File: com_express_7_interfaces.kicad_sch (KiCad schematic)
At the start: 8 parts, among them J11 Plug_Bus_CE7_EPT_401-51501-51

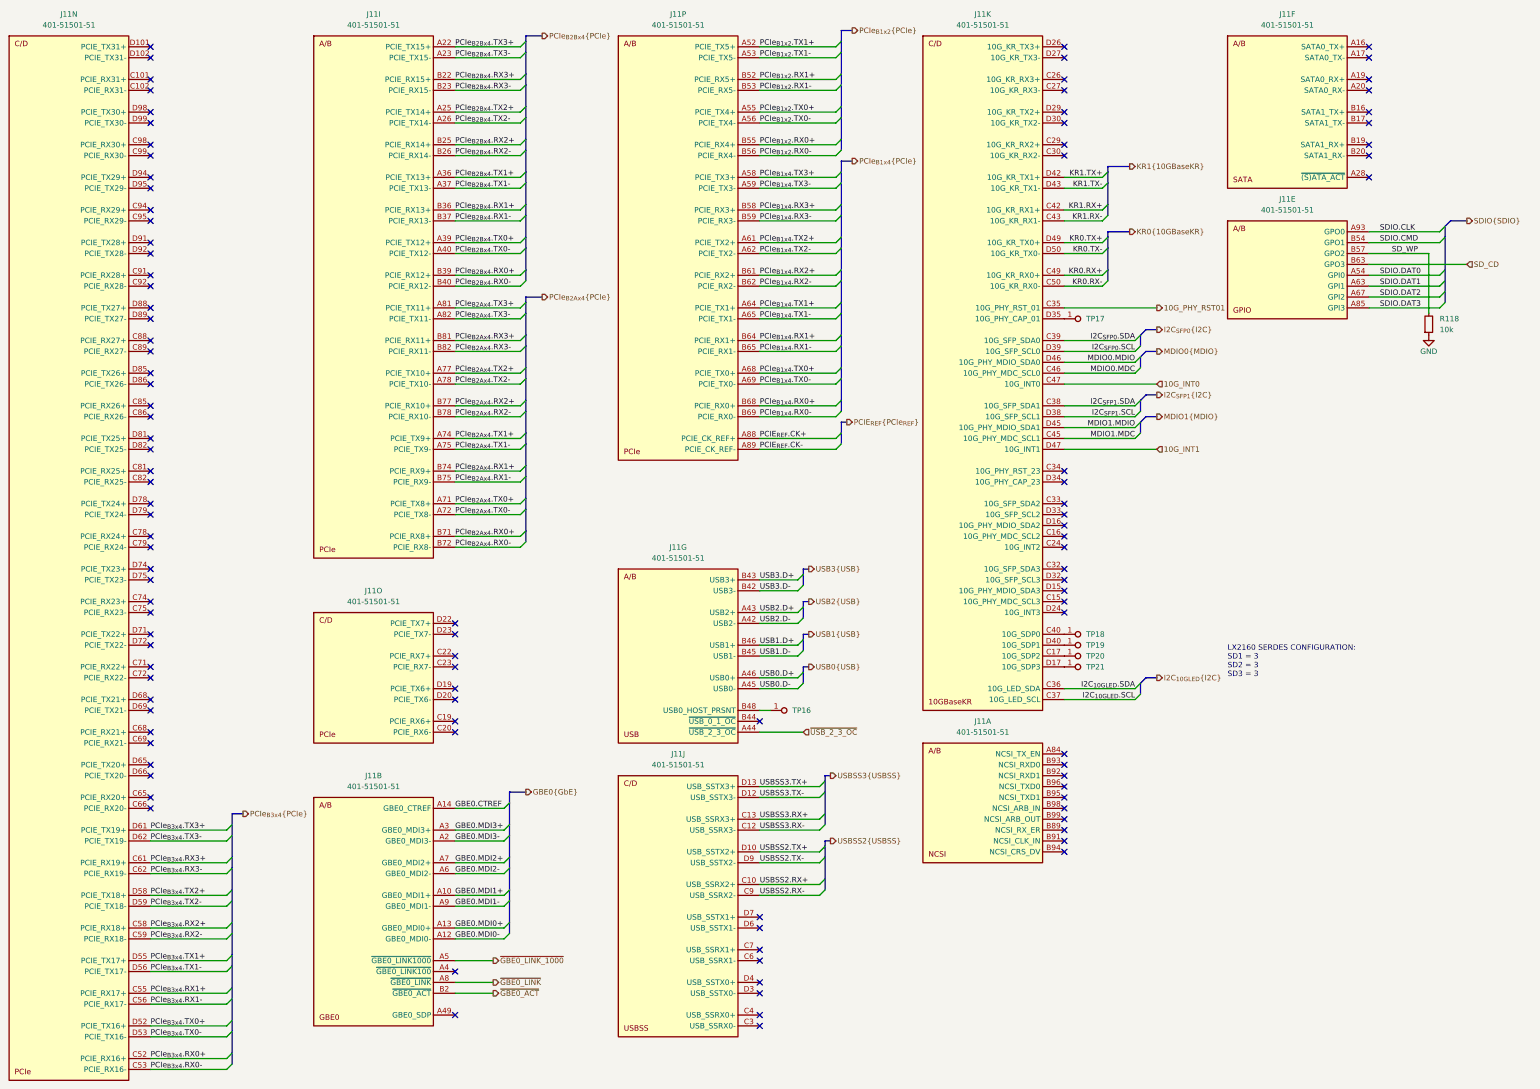
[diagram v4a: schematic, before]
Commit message: Reannotate schematic
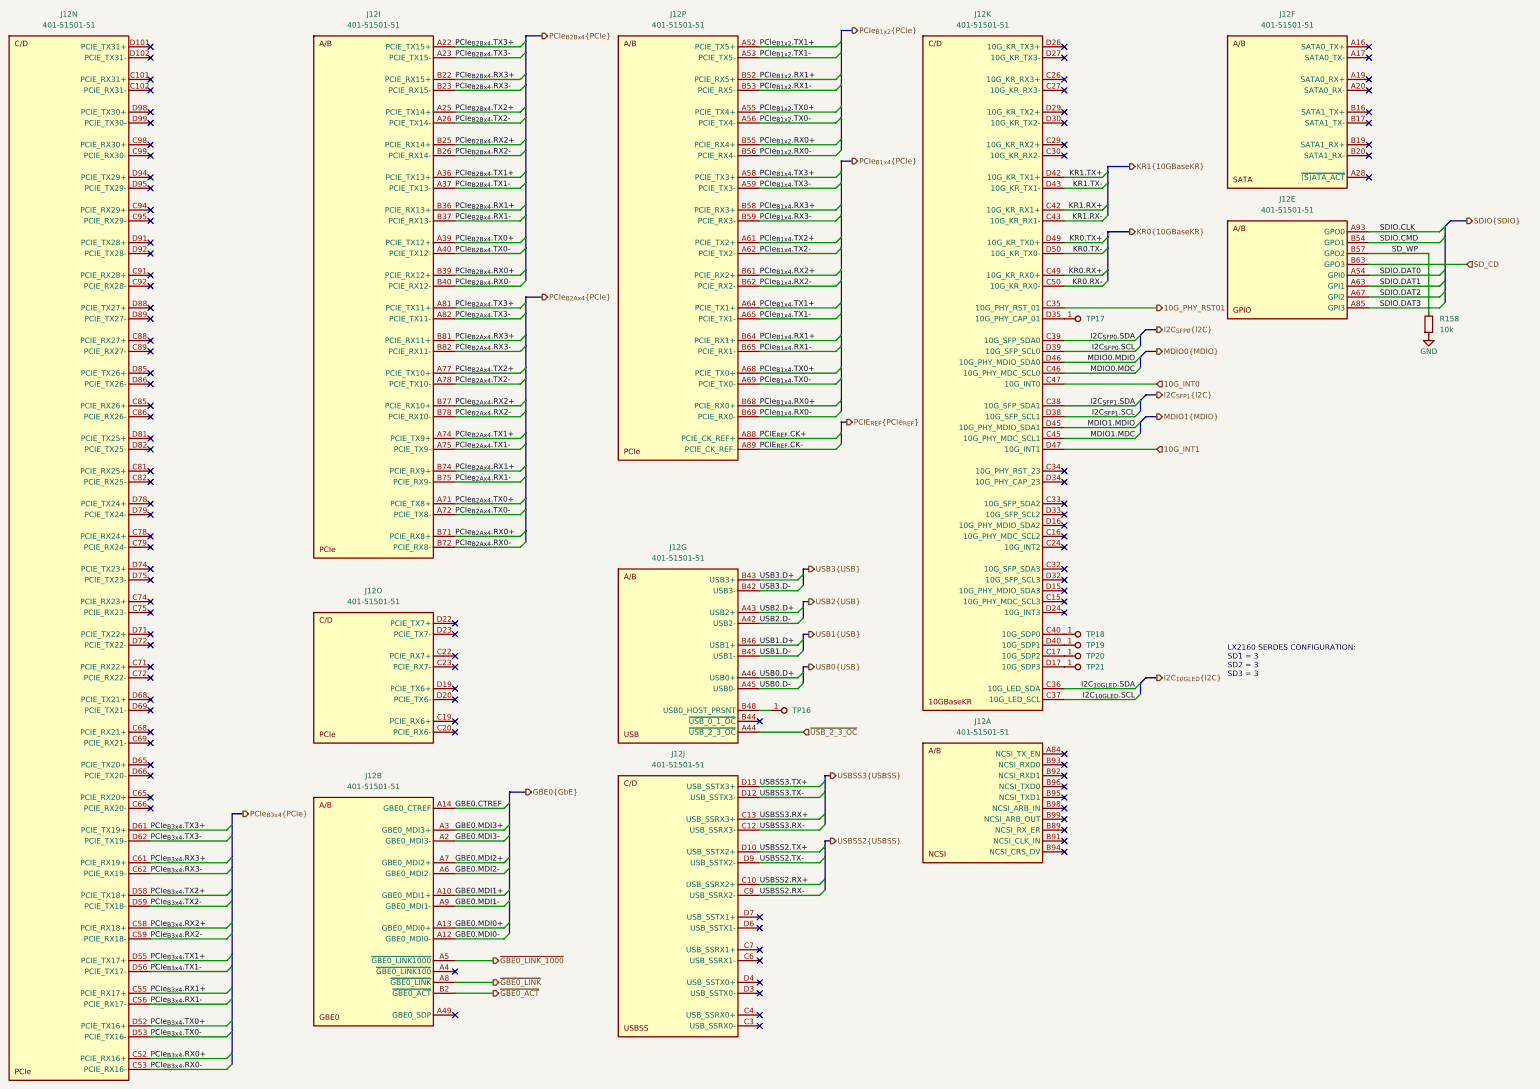
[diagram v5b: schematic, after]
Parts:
- renumbered J11 to J12, R118 to R158
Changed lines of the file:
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@@
   (symbol (lib_id "antmicroB2BConnectors:Plug_Bus_CE7_EPT_401-51501-51") (at 281.94 198.12 0) (unit 1)
     (in_bom yes) (on_board yes) (dnp no) (fields_autoplaced)
-    (property "Reference" "J11" (at 262.89 190.5 0)
+    (property "Reference" "J12" (at 262.89 190.5 0)
       (effects (font (size 1.27 1.27) (thickness 0.15)))
     )
@@
       (project "com-express-7-baseboard"
         (path "/1b8c34da-dad5-4b0b-8c4b-45db766c4dfa/d0206463-9f0a-4ce9-a6c7-202004597ed5"
-          (reference "J11") (unit 1)
+          (reference "J12") (unit 1)
         )
       )
@@
   (symbol (lib_id "antmicroB2BConnectors:Plug_Bus_CE7_EPT_401-51501-51") (at 281.94 33.02 0) (unit 11)
     (in_bom yes) (on_board yes) (dnp no) (fields_autoplaced)
-    (property "Reference" "J11" (at 262.89 25.4 0)
+    (property "Reference" "J12" (at 262.89 25.4 0)
       (effects (font (size 1.27 1.27) (thickness 0.15)))
     )
@@
       (project "com-express-7-baseboard"
         (path "/1b8c34da-dad5-4b0b-8c4b-45db766c4dfa/d0206463-9f0a-4ce9-a6c7-202004597ed5"
-          (reference "J11") (unit 11)
+          (reference "J12") (unit 11)
         )
       )
@@
   (symbol (lib_id "antmicroB2BConnectors:Plug_Bus_CE7_EPT_401-51501-51") (at 139.7 210.82 0) (unit 2)
     (in_bom yes) (on_board yes) (dnp no) (fields_autoplaced)
-    (property "Reference" "J11" (at 120.65 203.2 0)
+    (property "Reference" "J12" (at 120.65 203.2 0)
       (effects (font (size 1.27 1.27) (thickness 0.15)))
     )
@@
       (project "com-express-7-baseboard"
         (path "/1b8c34da-dad5-4b0b-8c4b-45db766c4dfa/d0206463-9f0a-4ce9-a6c7-202004597ed5"
-          (reference "J11") (unit 2)
+          (reference "J12") (unit 2)
         )
       )
@@
   (symbol (lib_id "antmicroB2BConnectors:Plug_Bus_CE7_EPT_401-51501-51") (at 353.06 33.02 0) (unit 6)
     (in_bom yes) (on_board yes) (dnp no) (fields_autoplaced)
-    (property "Reference" "J11" (at 334.01 25.4 0)
+    (property "Reference" "J12" (at 334.01 25.4 0)
       (effects (font (size 1.27 1.27) (thickness 0.15)))
     )
@@
       (project "com-express-7-baseboard"
         (path "/1b8c34da-dad5-4b0b-8c4b-45db766c4dfa/d0206463-9f0a-4ce9-a6c7-202004597ed5"
-          (reference "J11") (unit 6)
+          (reference "J12") (unit 6)
         )
       )
@@
   (symbol (lib_id "antmicroB2BConnectors:Plug_Bus_CE7_EPT_401-51501-51") (at 210.82 205.74 0) (unit 10)
     (in_bom yes) (on_board yes) (dnp no) (fields_autoplaced)
-    (property "Reference" "J11" (at 191.77 198.12 0)
+    (property "Reference" "J12" (at 191.77 198.12 0)
       (effects (font (size 1.27 1.27) (thickness 0.15)))
     )
@@
       (project "com-express-7-baseboard"
         (path "/1b8c34da-dad5-4b0b-8c4b-45db766c4dfa/d0206463-9f0a-4ce9-a6c7-202004597ed5"
-          (reference "J11") (unit 10)
+          (reference "J12") (unit 10)
         )
       )
@@
   (symbol (lib_id "antmicroResistors0402:R_10k_0402") (at 367.03 100.33 90) (unit 1)
     (in_bom yes) (on_board yes) (dnp no) (fields_autoplaced)
-    (property "Reference" "R118" (at 369.57 96.52 90)
+    (property "Reference" "R158" (at 369.57 96.52 90)
       (effects (font (size 1.27 1.27) (thickness 0.15)) (justify right))
     )
@@
       (project "com-express-7-baseboard"
         (path "/1b8c34da-dad5-4b0b-8c4b-45db766c4dfa/d0206463-9f0a-4ce9-a6c7-202004597ed5"
-          (reference "R118") (unit 1)
+          (reference "R158") (unit 1)
         )
       )
@@
   (symbol (lib_id "antmicroB2BConnectors:Plug_Bus_CE7_EPT_401-51501-51") (at 353.06 76.2 0) (unit 5)
     (in_bom yes) (on_board yes) (dnp no) (fields_autoplaced)
-    (property "Reference" "J11" (at 334.01 68.58 0)
+    (property "Reference" "J12" (at 334.01 68.58 0)
       (effects (font (size 1.27 1.27) (thickness 0.15)))
     )
@@
       (project "com-express-7-baseboard"
         (path "/1b8c34da-dad5-4b0b-8c4b-45db766c4dfa/d0206463-9f0a-4ce9-a6c7-202004597ed5"
-          (reference "J11") (unit 5)
+          (reference "J12") (unit 5)
         )
       )
@@
   (symbol (lib_id "antmicroB2BConnectors:Plug_Bus_CE7_EPT_401-51501-51") (at 210.82 157.48 0) (unit 7)
     (in_bom yes) (on_board yes) (dnp no) (fields_autoplaced)
-    (property "Reference" "J11" (at 191.77 149.86 0)
+    (property "Reference" "J12" (at 191.77 149.86 0)
       (effects (font (size 1.27 1.27) (thickness 0.15)))
     )
@@
       (project "com-express-7-baseboard"
         (path "/1b8c34da-dad5-4b0b-8c4b-45db766c4dfa/d0206463-9f0a-4ce9-a6c7-202004597ed5"
-          (reference "J11") (unit 7)
+          (reference "J12") (unit 7)
         )
       )
@@
   (symbol (lib_id "antmicropower:GND") (at 367.03 100.33 0) (unit 1)
     (in_bom yes) (on_board yes) (dnp no)
-    (property "Reference" "#PWR0147" (at 375.92 102.87 0)
+    (property "Reference" "#PWR0223" (at 375.92 102.87 0)
       (effects (font (size 1.27 1.27) (thickness 0.15)) (justify left bottom) hide)
     )
@@
       (project "com-express-7-baseboard"
         (path "/1b8c34da-dad5-4b0b-8c4b-45db766c4dfa/d0206463-9f0a-4ce9-a6c7-202004597ed5"
-          (reference "#PWR0147") (unit 1)
+          (reference "#PWR0223") (unit 1)
         )
       )
@@
   (symbol (lib_name "Plug_Bus_CE7_EPT_401-51501-51_1") (lib_id "antmicroB2BConnectors:Plug_Bus_CE7_EPT_401-51501-51") (at 139.7 33.02 0) (unit 9)
     (in_bom yes) (on_board yes) (dnp no) (fields_autoplaced)
-    (property "Reference" "J11" (at 120.65 25.4 0)
+    (property "Reference" "J12" (at 120.65 25.4 0)
       (effects (font (size 1.27 1.27) (thickness 0.15)))
     )
@@
       (project "com-express-7-baseboard"
         (path "/1b8c34da-dad5-4b0b-8c4b-45db766c4dfa/d0206463-9f0a-4ce9-a6c7-202004597ed5"
-          (reference "J11") (unit 9)
+          (reference "J12") (unit 9)
         )
       )
@@
   (symbol (lib_id "antmicroB2BConnectors:Plug_Bus_CE7_EPT_401-51501-51") (at 139.7 167.64 0) (unit 15)
     (in_bom yes) (on_board yes) (dnp no) (fields_autoplaced)
-    (property "Reference" "J11" (at 120.65 160.02 0)
+    (property "Reference" "J12" (at 120.65 160.02 0)
       (effects (font (size 1.27 1.27) (thickness 0.15)))
     )
@@
       (project "com-express-7-baseboard"
         (path "/1b8c34da-dad5-4b0b-8c4b-45db766c4dfa/d0206463-9f0a-4ce9-a6c7-202004597ed5"
-          (reference "J11") (unit 15)
+          (reference "J12") (unit 15)
         )
       )
@@
   (symbol (lib_id "antmicroB2BConnectors:Plug_Bus_CE7_EPT_401-51501-51") (at 68.58 33.02 0) (unit 14)
     (in_bom yes) (on_board yes) (dnp no) (fields_autoplaced)
-    (property "Reference" "J11" (at 49.53 25.4 0)
+    (property "Reference" "J12" (at 49.53 25.4 0)
       (effects (font (size 1.27 1.27) (thickness 0.15)))
     )
@@
       (project "com-express-7-baseboard"
         (path "/1b8c34da-dad5-4b0b-8c4b-45db766c4dfa/d0206463-9f0a-4ce9-a6c7-202004597ed5"
-          (reference "J11") (unit 14)
+          (reference "J12") (unit 14)
         )
       )
@@
   (symbol (lib_id "antmicroB2BConnectors:Plug_Bus_CE7_EPT_401-51501-51") (at 210.82 33.02 0) (unit 16)
     (in_bom yes) (on_board yes) (dnp no) (fields_autoplaced)
-    (property "Reference" "J11" (at 191.77 25.4 0)
+    (property "Reference" "J12" (at 191.77 25.4 0)
       (effects (font (size 1.27 1.27) (thickness 0.15)))
     )
@@
       (project "com-express-7-baseboard"
         (path "/1b8c34da-dad5-4b0b-8c4b-45db766c4dfa/d0206463-9f0a-4ce9-a6c7-202004597ed5"
-          (reference "J11") (unit 16)
+          (reference "J12") (unit 16)
         )
       )

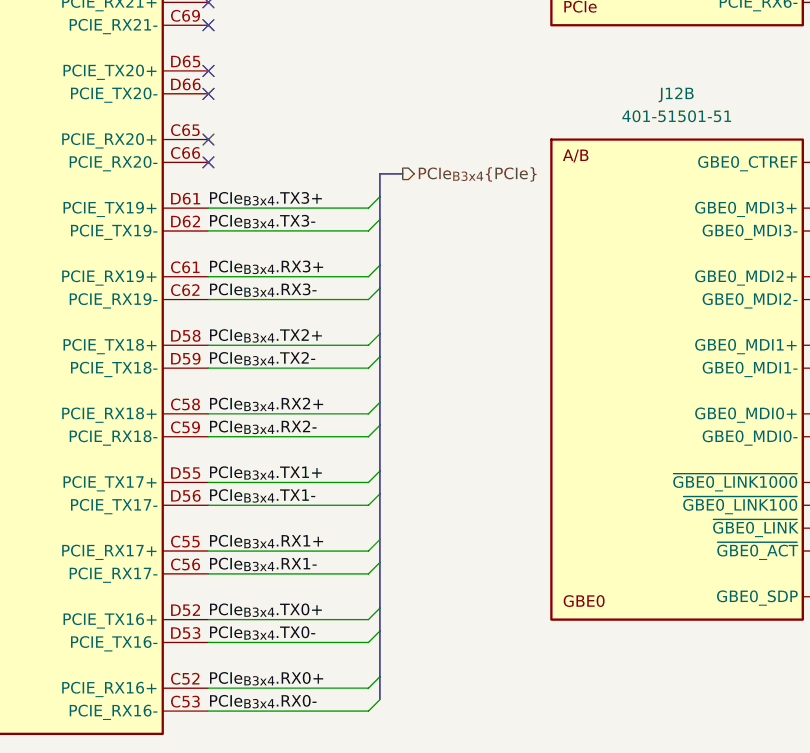
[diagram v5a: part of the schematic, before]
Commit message: [#58904] Fix DRC
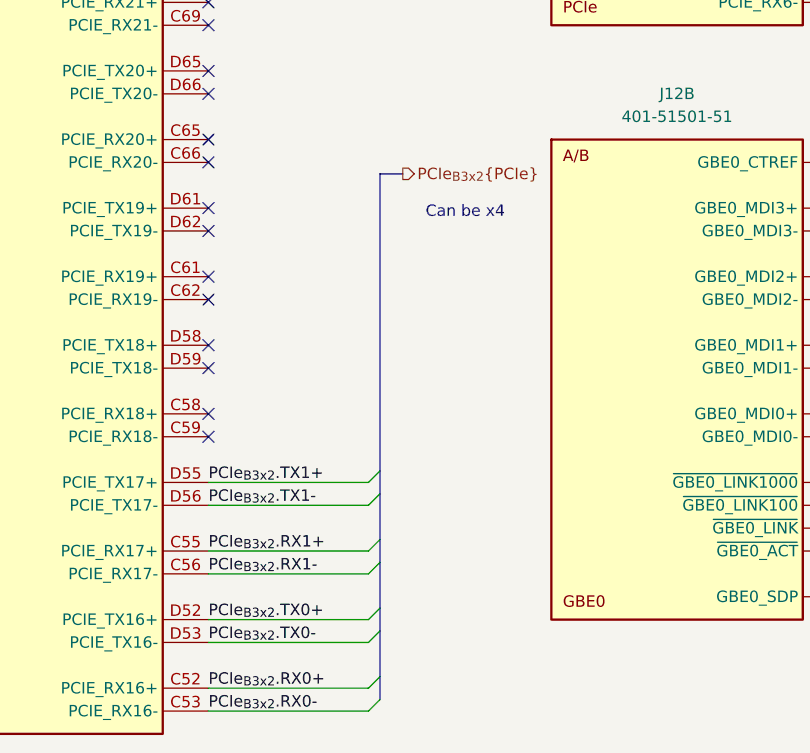
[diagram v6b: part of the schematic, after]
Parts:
- J12: Manufacturer EPT -> ept
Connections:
- net PCIe_{B3x4}.RX0+ renamed PCIe_{B3x2}.RX0+
- net PCIe_{B3x4}.RX0- renamed PCIe_{B3x2}.RX0-
- net PCIe_{B3x4}.RX1+ renamed PCIe_{B3x2}.RX1+
- net PCIe_{B3x4}.RX1- renamed PCIe_{B3x2}.RX1-
- net PCIe_{B3x4}.RX2+: no longer names the net of J12.C58 (PCIE_RX18+)
- net PCIe_{B3x4}.RX2-: no longer names the net of J12.C59 (PCIE_RX18-)
- net PCIe_{B3x4}.RX3+: no longer names the net of J12.C61 (PCIE_RX19+)
- net PCIe_{B3x4}.RX3-: no longer names the net of J12.C62 (PCIE_RX19-)
- net PCIe_{B3x4}.TX0+ renamed PCIe_{B3x2}.TX0+
- net PCIe_{B3x4}.TX0- renamed PCIe_{B3x2}.TX0-
- net PCIe_{B3x4}.TX1+ renamed PCIe_{B3x2}.TX1+
- net PCIe_{B3x4}.TX1- renamed PCIe_{B3x2}.TX1-
- net PCIe_{B3x4}.TX2+: no longer names the net of J12.D58 (PCIE_TX18+)
- net PCIe_{B3x4}.TX2-: no longer names the net of J12.D59 (PCIE_TX18-)
- net PCIe_{B3x4}.TX3+: no longer names the net of J12.D61 (PCIE_TX19+)
- net PCIe_{B3x4}.TX3-: no longer names the net of J12.D62 (PCIE_TX19-)
- no-connect marks 106 -> 114
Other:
- note added: "Can be x4"

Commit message: Update components from the library
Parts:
- R158, TP16, TP17, TP18, TP19, TP20, TP21: Public (none) -> False
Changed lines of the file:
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@@
       (effects (font (size 1.27 1.27) (thickness 0.15)) (justify left bottom) hide)
     )
+    (property "Public" "False" (at 292.1 189.23 0)
+      (effects (font (size 1.27 1.27)) (justify left bottom) hide)
+    )
     (pin "1")
     (instances
@@
       (effects (font (size 1.27 1.27)) (justify left bottom) hide)
     )
+    (property "Public" "False" (at 397.51 80.01 0)
+      (effects (font (size 1.27 1.27)) (justify left bottom) hide)
+    )
     (pin "2")
     (pin "1")
@@
       (effects (font (size 1.27 1.27) (thickness 0.15)) (justify left bottom) hide)
     )
+    (property "Public" "False" (at 292.1 186.69 0)
+      (effects (font (size 1.27 1.27)) (justify left bottom) hide)
+    )
     (pin "1")
     (instances
@@
       (effects (font (size 1.27 1.27) (thickness 0.15)) (justify left bottom) hide)
     )
+    (property "Public" "False" (at 292.1 110.49 0)
+      (effects (font (size 1.27 1.27)) (justify left bottom) hide)
+    )
     (pin "1")
     (instances
@@
       (effects (font (size 1.27 1.27) (thickness 0.15)) (justify left bottom) hide)
     )
+    (property "Public" "False" (at 292.1 191.77 0)
+      (effects (font (size 1.27 1.27)) (justify left bottom) hide)
+    )
     (pin "1")
     (instances
@@
       (effects (font (size 1.27 1.27) (thickness 0.15)) (justify left bottom) hide)
     )
+    (property "Public" "False" (at 292.1 184.15 0)
+      (effects (font (size 1.27 1.27)) (justify left bottom) hide)
+    )
     (pin "1")
     (instances
@@
       (effects (font (size 1.27 1.27) (thickness 0.15)) (justify left bottom) hide)
     )
+    (property "Public" "False" (at 223.52 201.93 0)
+      (effects (font (size 1.27 1.27)) (justify left bottom) hide)
+    )
     (pin "1")
